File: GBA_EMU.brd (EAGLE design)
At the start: 130.7 x 72.9 mm, 63 parts, among them J1 USB-MINIB-5PIN, Q1 MOSFET-PCHANNEL, SW1 LEFT, SW2 RIGHT, SW3 PWR_SWITCH, U2 FT230X, U4 LM4875, U5 V_REG_LDOSMD2, U7 AZV321, X2 HEADPHONE

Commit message: updated pdf render
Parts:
- moved U$4 1.52 mm to (29.0, 24.4)
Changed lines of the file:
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@@
 <element name="U$1" library="custom" package="S020-75MM" value="CBT3244AD" x="80.16" y="51.844" rot="R90"/>
 <element name="POT1" library="adafruit" package="THUMBWHEEL" value="THUMBPOT" x="91.2908" y="26.0612" rot="R195"/>
-<element name="U$4" library="custom" package="254SA103B50A" value="CTS254_JOYSTICKSM" x="27.432" y="24.384"/>
+<element name="U$4" library="custom" package="254SA103B50A" value="CTS254_JOYSTICKSM" x="28.956" y="24.384"/>
 <element name="SW4" library="adafruit" package="TACT_PANA-EVQ" value="" x="45.212" y="69.596"/>
 <element name="SW5" library="adafruit" package="TACT_PANA-EVQ" value="" x="121.412" y="69.596"/>
@@
 <wire x1="91.125" y1="73.025" x2="97.31125" y2="64.77" width="0" layer="19" extent="16-16"/>
 <wire x1="84.29875" y1="74.850625" x2="91.125" y2="73.025" width="0" layer="19" extent="16-16"/>
-<wire x1="33.932" y1="36.184" x2="26.782" y2="28.184" width="0" layer="19" extent="1-1"/>
-<wire x1="37.677790625" y1="45.56770625" x2="33.932" y2="36.184" width="0" layer="19" extent="1-1"/>
+<wire x1="35.456" y1="36.184" x2="28.306" y2="28.184" width="0" layer="19" extent="1-1"/>
+<wire x1="37.677790625" y1="45.56770625" x2="35.456" y2="36.184" width="0" layer="19" extent="1-1"/>
 <wire x1="29.69269375" y1="53.293165625" x2="37.677790625" y2="45.56770625" width="0" layer="19" extent="1-1"/>
 <wire x1="37.737625" y1="61.42204375" x2="45.69403125" y2="53.50889375" width="0" layer="19" extent="1-1"/>
 <wire x1="147" y1="28.575" x2="133.178471875" y2="27.330959375" width="0" layer="19" extent="16-16"/>
-<wire x1="125.524" y1="60.452" x2="36.632" y2="23.384" width="0" layer="19" extent="1-1"/>
+<wire x1="125.524" y1="60.452" x2="38.156" y2="23.384" width="0" layer="19" extent="1-1"/>
 <wire x1="139.24" y1="62.484" x2="125.524" y2="60.452" width="0" layer="19" extent="1-1"/>
 </signal>
@@
 <contactref element="U$4" pad="P$4"/>
 <contactref element="U$4" pad="P$5"/>
-<wire x1="31.232" y1="23.384" x2="26.782" y2="33.584" width="0" layer="19" extent="1-1"/>
-<wire x1="33.932" y1="23.384" x2="31.232" y2="23.384" width="0" layer="19" extent="1-1"/>
+<wire x1="32.756" y1="23.384" x2="28.306" y2="33.584" width="0" layer="19" extent="1-1"/>
+<wire x1="35.456" y1="23.384" x2="32.756" y2="23.384" width="0" layer="19" extent="1-1"/>
 </signal>
 <signal name="Z_BTN">

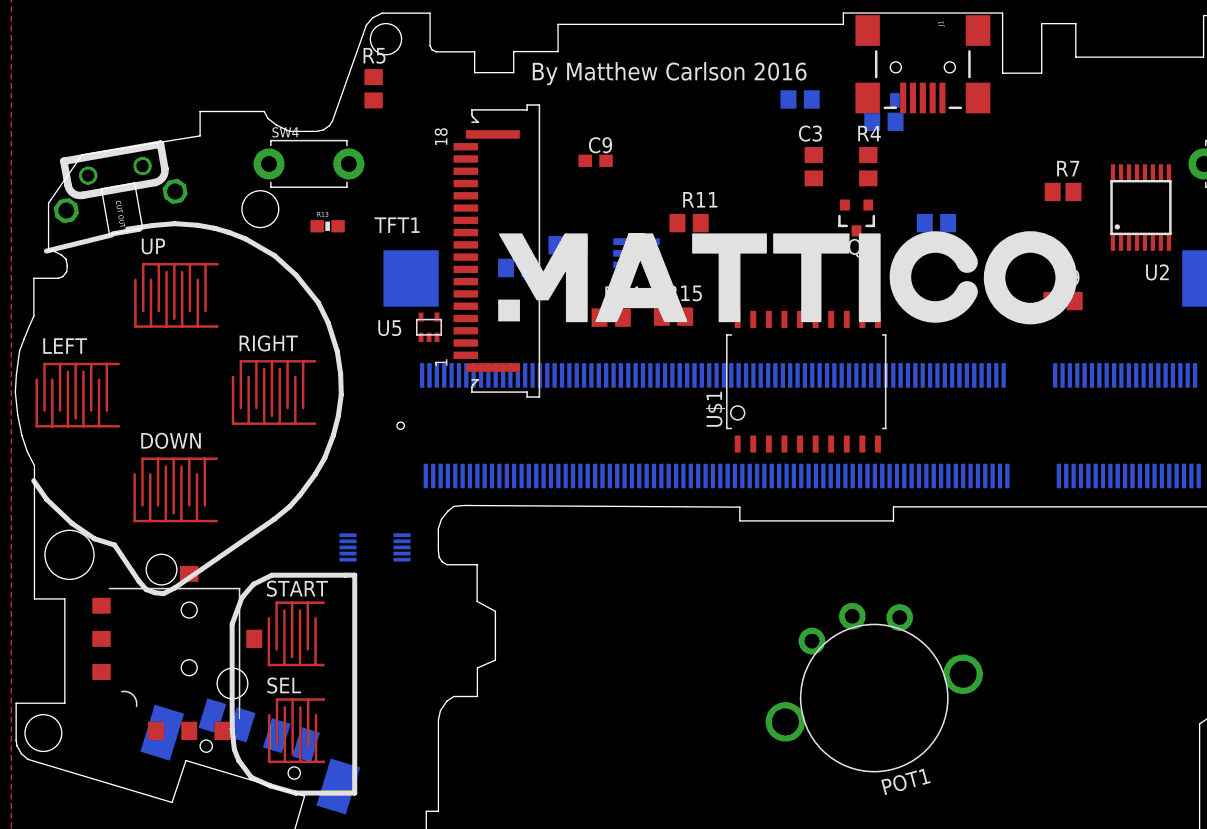
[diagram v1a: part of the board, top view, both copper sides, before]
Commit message: added co processor and usb hub chip
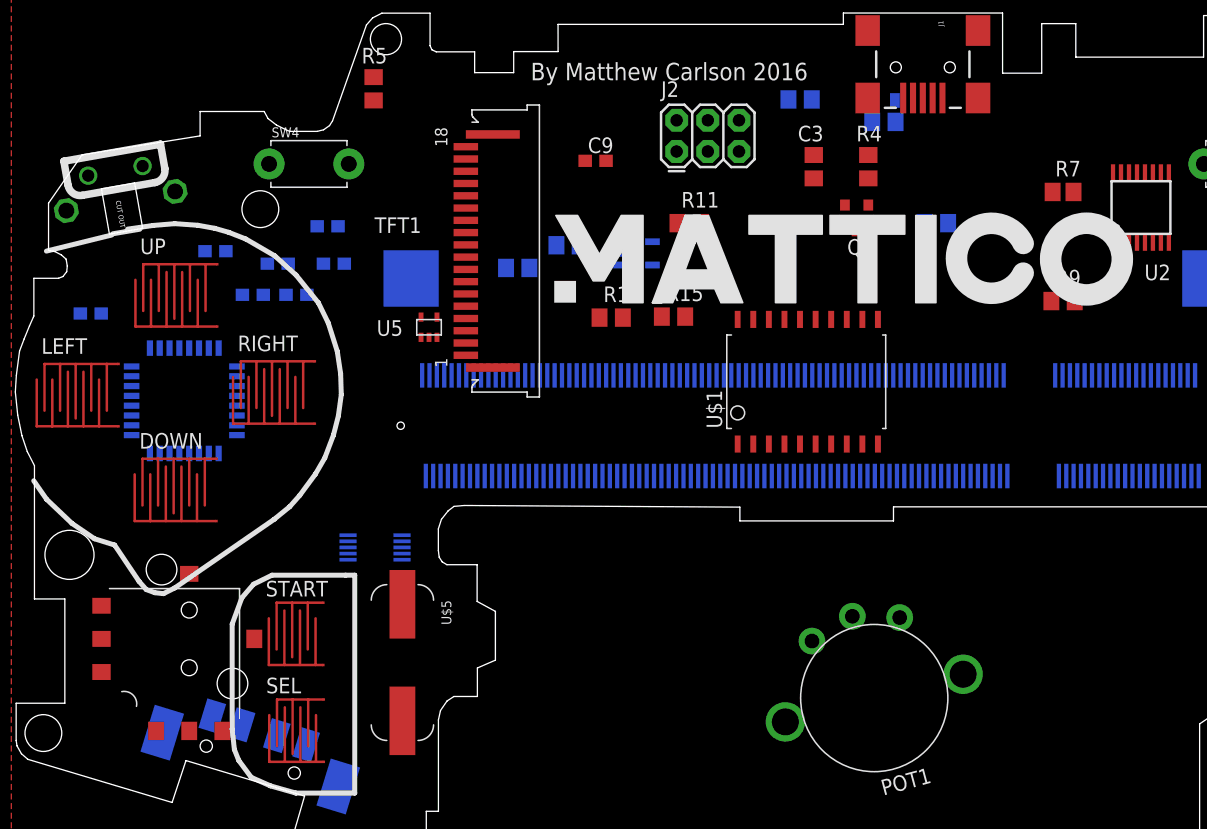
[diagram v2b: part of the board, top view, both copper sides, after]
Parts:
- added C10: 1.0uF, SparkFun-Capacitors:0603-CAP
- added C11, C12: 22pF, SparkFun-Capacitors:0603-CAP
- added COPRO: MEGA16u2, adafruit:TQFP32-08
- added J2: AVR_SPI, SparkFun-Connectors:2X3
- added R17, R18: 22, SparkFun-Resistors:0603-RES
- added R19: 10K, SparkFun-Resistors:0603-RES
- added U$5: CRYSTAL-ABLS, custom:HC49/US
- added U$7: LOGO2INCH_SVG, custom:LOGO_2INCH_SVG
- moved U$2 4.82 mm to (64.6, 57.5)
- flipped R13 to the bottom, turned to 180 degrees
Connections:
- new net COPRO_MISO: COPRO.17, J2.1
- new net COPRO_MOSI: COPRO.16, J2.4
- new net COPRO_RESET: COPRO.24, J2.5, R19.1
- new net COPRO_SCK: COPRO.15, J2.3
- new net N$19: COPRO.30, R17.2
- new net N$22: COPRO.29, R18.2
- new net N$25: C10.1, COPRO.27
- new net N$28: C11.1, COPRO.1, U$5.P$2
- new net N$29: C12.1, COPRO.2, U$5.P$1
- net 5V: now also COPRO.31, COPRO.32, COPRO.4, J2.2, R19.2
- net GND: now also C10.2, C11.2, C12.2, COPRO.28, COPRO.3, J2.6

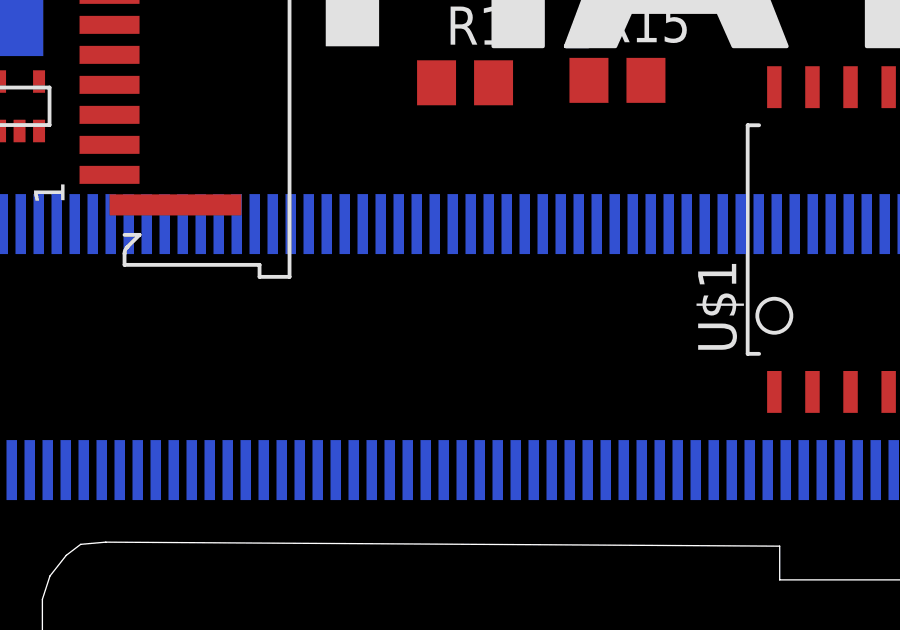
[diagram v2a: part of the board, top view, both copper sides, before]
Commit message: added usb hub chip :)
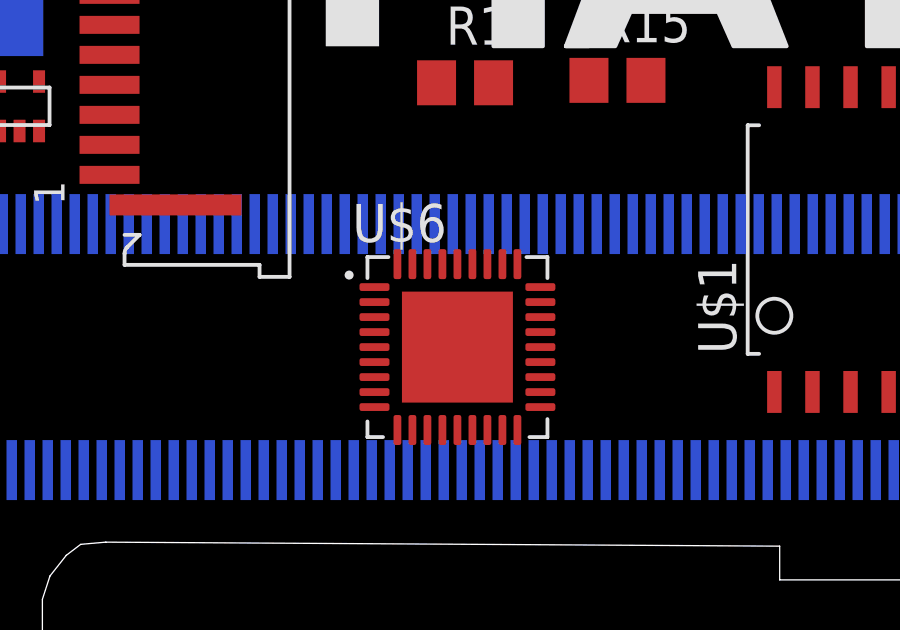
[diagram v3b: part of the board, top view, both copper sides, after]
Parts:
- added U$6: USB2523B, custom:QFN37P50_600X600X100L62X24T370N
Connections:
- net 3.3V: now also U$6.10, U$6.15, U$6.23, U$6.29, U$6.36, U$6.5
- net GND: now also U$6.37
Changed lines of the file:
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@@
 </element>
 <element name="U$7" library="custom" package="LOGO_2INCH_SVG" value="LOGO2INCH_SVG" x="112.324" y="57.016" rot="MR0"/>
+<element name="U$6" library="custom" package="QFN37P50_600X600X100L62X24T370N" value="USB2523B" x="69.596" y="48.26"/>
 </elements>
 <signals>
@@
 <contactref element="COPRO" pad="28"/>
 <contactref element="J2" pad="6"/>
+<contactref element="U$6" pad="37"/>
 <wire x1="139.24" y1="62.484" x2="141.835725" y2="50.90233125" width="0" layer="19" extent="1-1"/>
 <wire x1="90.74" y1="44.16" x2="91.59" y2="46.764" width="0" layer="19" extent="1-16"/>
@@
 <wire x1="97.31125" y1="64.77" x2="91.125" y2="73.025" width="0" layer="19" extent="16-16"/>
 <wire x1="147" y1="28.575" x2="133.178471875" y2="27.330959375" width="0" layer="19" extent="16-16"/>
+<wire x1="69.596" y1="48.26" x2="38.156" y2="23.384" width="0" layer="19" extent="1-1"/>
 </signal>
 <signal name="TXD">
@@
 <contactref element="U$3" pad="1"/>
 <contactref element="R13" pad="2"/>
+<contactref element="U$6" pad="5"/>
+<contactref element="U$6" pad="10"/>
+<contactref element="U$6" pad="36"/>
+<contactref element="U$6" pad="15"/>
+<contactref element="U$6" pad="29"/>
+<contactref element="U$6" pad="23"/>
 <wire x1="106.34" y1="44.16" x2="107.53" y2="67.31" width="0" layer="19" extent="1-16"/>
 <wire x1="57.14" y1="44.16" x2="106.34" y2="44.16" width="0" layer="19" extent="16-16"/>
@@
 <wire x1="48.4" y1="37.336" x2="56.54" y2="44.16" width="0" layer="19" extent="16-16"/>
 <wire x1="47.586" y1="64.516" x2="56.24" y2="52.36" width="0" layer="19" extent="16-16"/>
+<wire x1="71.096" y1="51.025" x2="48.4" y2="37.336" width="0" layer="19" extent="1-16"/>
+<wire x1="72.361" y1="48.26" x2="71.096" y2="51.025" width="0" layer="19" extent="1-1"/>
+<wire x1="67.596" y1="51.025" x2="71.096" y2="51.025" width="0" layer="19" extent="1-1"/>
+<wire x1="66.831" y1="48.26" x2="67.596" y2="51.025" width="0" layer="19" extent="1-1"/>
+<wire x1="67.596" y1="45.495" x2="66.831" y2="48.26" width="0" layer="19" extent="1-1"/>
+<wire x1="70.096" y1="45.495" x2="67.596" y2="45.495" width="0" layer="19" extent="1-1"/>
 </signal>
 <signal name="1.8V">
